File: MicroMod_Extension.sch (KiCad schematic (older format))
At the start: 79 parts, among them J1 2199230-4, J11 Screw_Terminal_01x04, J2 XKB_U262-16XN-4BVC11, J3 RSP-122811-01, J4 Screw_Terminal_01x04, J5 Conn_01x08, J6 Conn_01x08, J7 Conn_01x04, J8 Conn_01x04, J9 Conn_01x04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

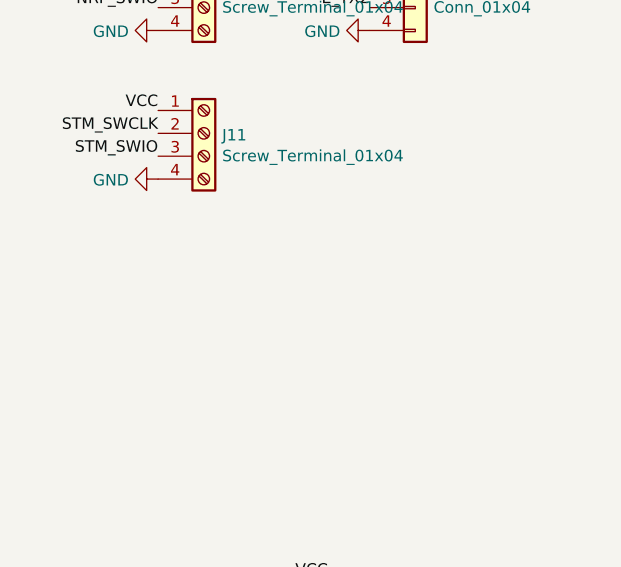
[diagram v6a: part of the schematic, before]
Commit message: add i2c connector
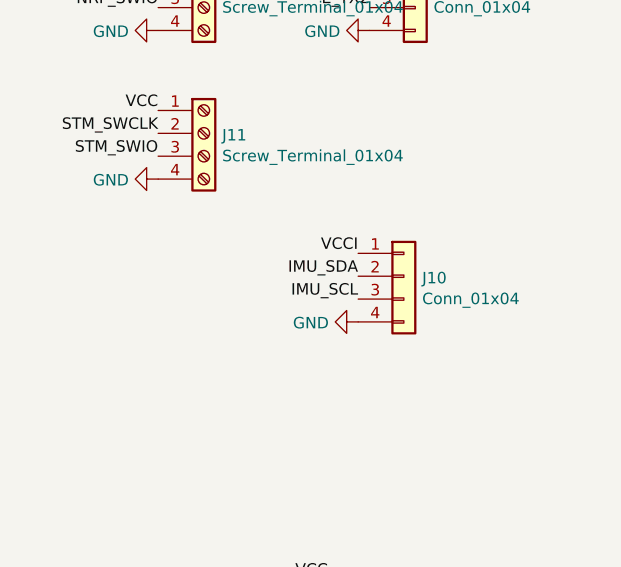
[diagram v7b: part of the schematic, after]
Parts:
- added J10: Conn_01x04, Connector_JST:JST_SUR_SM04B-SURS-TF_1x04-1MP_P0.80mm_Horizontal, symbol Connector_Generic:Conn_01x04
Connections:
- net GND: now also J10.4 (Pin_4)
- net IMU_SCL: now also J10.3 (Pin_3)
- net IMU_SDA: now also J10.2 (Pin_2)
- net VCCI: now also J10.1 (Pin_1)
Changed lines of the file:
@@
 NoConn ~ 12050 2825
 NoConn ~ 12050 1925
-NoConn ~ 5625 5975
-NoConn ~ 4425 5975
-NoConn ~ 4425 6675
-NoConn ~ 4425 6775
-Wire Wire Line
-	5625 6975 5725 6975
-Wire Wire Line
-	5725 6975 5725 7075
-Wire Wire Line
-	5625 7075 5725 7075
-Connection ~ 5725 7075
-Wire Wire Line
-	5725 7075 5725 7225
-$Comp
-L power:GND #PWR0131
-U 1 1 619EDD8D
-P 5725 7300
-F 0 "#PWR0131" H 5725 7050 50  0001 C CNN
-F 1 "GND" V 5730 7172 50  0000 R CNN
-F 2 "" H 5725 7300 50  0001 C CNN
-F 3 "" H 5725 7300 50  0001 C CNN
-	1    5725 7300
-	1    0    0    -1
-$EndComp
-Wire Wire Line
-	5625 5775 5675 5775
-Wire Wire Line
-	5675 5675 5625 5675
-Wire Wire Line
-	5675 5675 5850 5675
-Connection ~ 5675 5675
-$Comp
-L Device:C C1
-U 1 1 61A296B8
-P 5850 5825
-F 0 "C1" H 5875 5725 50  0000 L CNN
-F 1 "100n" H 5875 5650 50  0000 L CNN
-F 2 "Capacitor_SMD:C_0402_1005Metric" H 5888 5675 50  0001 C CNN
-F 3 "~" H 5850 5825 50  0001 C CNN
-	1    5850 5825
-	1    0    0    -1
-$EndComp
-Wire Wire Line
-	5725 6975 5725 6300
-Wire Wire Line
-	5725 6300 5850 6300
-Wire Wire Line
-	5850 6300 5850 5975
-Connection ~ 5725 6975
-Text Label 6225 5675 0    50   ~ 0
-VCCI
-Wire Wire Line
-	5675 5775 5675 5675
-Text Label 4425 6375 2    50   ~ 0
-SPI2_MOSI
-Text Label 4425 6275 2    50   ~ 0
-SPI2_SCK
-Connection ~ 5725 7225
-Wire Wire Line
-	5725 7225 5725 7300
-Text Label 5625 6775 0    50   ~ 0
-INT_GYR
-NoConn ~ 5625 6675
 Wire Wire Line
 	10550 9100 11425 9100
@@
 Text Label 12175 9100 0    50   ~ 0
 VCCI
-$Comp
-L MicroMod_Extension:BMP384 U8
-U 1 1 61BB569C
-P 6425 6350
-F 0 "U8" V 5975 5575 50  0000 C CNN
-F 1 "BMP384" V 5900 5475 50  0000 C CNN
-F 2 "MicroMod_Extension:PQFN45P200X200X100-10N" H 6275 6600 50  0001 C CNN
-F 3 "" H 6275 6600 50  0001 C CNN
-	1    6425 6350
-	0    -1   -1   0
-$EndComp
-Wire Wire Line
-	6475 6300 6475 5900
-Wire Wire Line
-	6475 5900 6775 5900
-Connection ~ 6475 5900
-$Comp
-L Device:C C23
-U 1 1 61BEE553
-P 6225 5825
-F 0 "C23" H 6125 5925 50  0000 L CNN
-F 1 "100n" H 6025 6000 50  0000 L CNN
-F 2 "Capacitor_SMD:C_0402_1005Metric" H 6263 5675 50  0001 C CNN
-F 3 "~" H 6225 5825 50  0001 C CNN
-	1    6225 5825
-	-1   0    0    1
-$EndComp
-Wire Wire Line
-	7075 5900 6925 5900
-Connection ~ 7075 5900
-NoConn ~ 7325 6250
-Text Label 6475 6500 2    50   ~ 0
-IMU_SCL
-Text Label 6925 6850 3    50   ~ 0
-IMU_SDA
-Wire Wire Line
-	7325 6500 7400 6500
-$Comp
-L power:GND #PWR0132
-U 1 1 61DA92BC
-P 7675 5900
-F 0 "#PWR0132" H 7675 5650 50  0001 C CNN
-F 1 "GND" V 7680 5772 50  0000 R CNN
-F 2 "" H 7675 5900 50  0001 C CNN
-F 3 "" H 7675 5900 50  0001 C CNN
-	1    7675 5900
-	0    -1   -1   0
-$EndComp
-Wire Wire Line
-	5850 5675 6225 5675
-Connection ~ 5850 5675
-Connection ~ 6475 5675
-Wire Wire Line
-	6475 5675 6475 5800
-Wire Wire Line
-	6475 5675 7400 5675
-Connection ~ 6225 5675
-Wire Wire Line
-	6225 5675 6475 5675
-Wire Wire Line
-	7075 5900 7675 5900
-Wire Wire Line
-	6225 5975 6225 6300
-Wire Wire Line
-	6225 6300 5850 6300
-Connection ~ 5850 6300
-Wire Wire Line
-	6775 6850 6775 7225
-$Comp
-L Device:C C24
-U 1 1 61EF129D
-P 6850 5800
-F 0 "C24" H 6750 5900 50  0000 L CNN
-F 1 "100n" H 6650 5975 50  0000 L CNN
-F 2 "Capacitor_SMD:C_0402_1005Metric" H 6888 5650 50  0001 C CNN
-F 3 "~" H 6850 5800 50  0001 C CNN
-	1    6850 5800
-	0    1    1    0
-$EndComp
-Wire Wire Line
-	6475 5800 6700 5800
-Connection ~ 6475 5800
-Wire Wire Line
-	6475 5800 6475 5900
-Wire Wire Line
-	7400 5675 7400 6500
-Wire Wire Line
-	7000 5800 7075 5800
-Wire Wire Line
-	7075 5800 7075 5900
-Wire Wire Line
-	6775 7225 5725 7225
-Wire Wire Line
-	7075 6850 7075 7025
-Wire Wire Line
-	7075 7025 7400 7025
-Wire Wire Line
-	7400 7025 7400 6500
-Connection ~ 7400 6500
 Connection ~ 2050 7200
 Connection ~ 2050 7000
@@
 	1    0    0    -1
 $EndComp
-Text Label 4425 6475 2    50   ~ 0
-SPI2_MISO
+Text Label 15225 2275 2    50   ~ 0
+C4
+NoConn ~ 15225 2375
+Text Label 4425 6075 2    50   ~ 0
+C13
 $Comp
 L MicroMod_Extension:BMI270 U7
@@
 	1    0    0    -1
 $EndComp
-Text Label 4425 6075 2    50   ~ 0
-C13
-Text Label 15225 2275 2    50   ~ 0
-C4
-NoConn ~ 15225 2375
+Text Label 4425 6475 2    50   ~ 0
+SPI2_MISO
+Connection ~ 7400 6500
+Wire Wire Line
+	7400 7025 7400 6500
+Wire Wire Line
+	7075 7025 7400 7025
+Wire Wire Line
+	7075 6850 7075 7025
+Wire Wire Line
+	6775 7225 5725 7225
+Wire Wire Line
+	7075 5800 7075 5900
+Wire Wire Line
+	7000 5800 7075 5800
+Wire Wire Line
+	7400 5675 7400 6500
+Wire Wire Line
+	6475 5800 6475 5900
+Connection ~ 6475 5800
+Wire Wire Line
+	6475 5800 6700 5800
+$Comp
+L Device:C C24
+U 1 1 61EF129D
+P 6850 5800
+F 0 "C24" H 6750 5900 50  0000 L CNN
+F 1 "100n" H 6650 5975 50  0000 L CNN
+F 2 "Capacitor_SMD:C_0402_1005Metric" H 6888 5650 50  0001 C CNN
+F 3 "~" H 6850 5800 50  0001 C CNN
+	1    6850 5800
+	0    1    1    0
+$EndComp
+Wire Wire Line
+	6775 6850 6775 7225
+Connection ~ 5850 6300
+Wire Wire Line
+	6225 6300 5850 6300
+Wire Wire Line
+	6225 5975 6225 6300
+Wire Wire Line
+	7075 5900 7675 5900
+Wire Wire Line
+	6225 5675 6475 5675
+Connection ~ 6225 5675
+Wire Wire Line
+	6475 5675 7400 5675
+Wire Wire Line
+	6475 5675 6475 5800
+Connection ~ 6475 5675
+Connection ~ 5850 5675
+Wire Wire Line
+	5850 5675 6225 5675
+$Comp
+L power:GND #PWR0132
+U 1 1 61DA92BC
+P 7675 5900
+F 0 "#PWR0132" H 7675 5650 50  0001 C CNN
+F 1 "GND" V 7680 5772 50  0000 R CNN
+F 2 "" H 7675 5900 50  0001 C CNN
+F 3 "" H 7675 5900 50  0001 C CNN
+	1    7675 5900
+	0    -1   -1   0
+$EndComp
+Wire Wire Line
+	7325 6500 7400 6500
+Text Label 6925 6850 3    50   ~ 0
+IMU_SDA
+Text Label 6475 6500 2    50   ~ 0
+IMU_SCL
+NoConn ~ 7325 6250
+Connection ~ 7075 5900
+Wire Wire Line
+	7075 5900 6925 5900
+$Comp
+L Device:C C23
+U 1 1 61BEE553
+P 6225 5825
+F 0 "C23" H 6125 5925 50  0000 L CNN
+F 1 "100n" H 6025 6000 50  0000 L CNN
+F 2 "Capacitor_SMD:C_0402_1005Metric" H 6263 5675 50  0001 C CNN
+F 3 "~" H 6225 5825 50  0001 C CNN
+	1    6225 5825
+	-1   0    0    1
+$EndComp
+Connection ~ 6475 5900
+Wire Wire Line
+	6475 5900 6775 5900
+Wire Wire Line
+	6475 6300 6475 5900
+$Comp
+L MicroMod_Extension:BMP384 U8
+U 1 1 61BB569C
+P 6425 6350
+F 0 "U8" V 5975 5575 50  0000 C CNN
+F 1 "BMP384" V 5900 5475 50  0000 C CNN
+F 2 "MicroMod_Extension:PQFN45P200X200X100-10N" H 6275 6600 50  0001 C CNN
+F 3 "" H 6275 6600 50  0001 C CNN
+	1    6425 6350
+	0    -1   -1   0
+$EndComp
+NoConn ~ 5625 6675
+Text Label 5625 6775 0    50   ~ 0
+INT_GYR
+Wire Wire Line
+	5725 7225 5725 7300
+Connection ~ 5725 7225
+Text Label 4425 6275 2    50   ~ 0
+SPI2_SCK
+Text Label 4425 6375 2    50   ~ 0
+SPI2_MOSI
+Wire Wire Line
+	5675 5775 5675 5675
+Text Label 6225 5675 0    50   ~ 0
+VCCI
+Connection ~ 5725 6975
+Wire Wire Line
+	5850 6300 5850 5975
+Wire Wire Line
+	5725 6300 5850 6300
+Wire Wire Line
+	5725 6975 5725 6300
+$Comp
+L Device:C C1
+U 1 1 61A296B8
+P 5850 5825
+F 0 "C1" H 5875 5725 50  0000 L CNN
+F 1 "100n" H 5875 5650 50  0000 L CNN
+F 2 "Capacitor_SMD:C_0402_1005Metric" H 5888 5675 50  0001 C CNN
+F 3 "~" H 5850 5825 50  0001 C CNN
+	1    5850 5825
+	1    0    0    -1
+$EndComp
+Connection ~ 5675 5675
+Wire Wire Line
+	5675 5675 5850 5675
+Wire Wire Line
+	5675 5675 5625 5675
+Wire Wire Line
+	5625 5775 5675 5775
+$Comp
+L power:GND #PWR0131
+U 1 1 619EDD8D
+P 5725 7300
+F 0 "#PWR0131" H 5725 7050 50  0001 C CNN
+F 1 "GND" V 5730 7172 50  0000 R CNN
+F 2 "" H 5725 7300 50  0001 C CNN
+F 3 "" H 5725 7300 50  0001 C CNN
+	1    5725 7300
+	1    0    0    -1
+$EndComp
+Wire Wire Line
+	5725 7075 5725 7225
+Connection ~ 5725 7075
+Wire Wire Line
+	5625 7075 5725 7075
+Wire Wire Line
+	5725 6975 5725 7075
+Wire Wire Line
+	5625 6975 5725 6975
+NoConn ~ 4425 6775
+NoConn ~ 4425 6675
+NoConn ~ 4425 5975
+NoConn ~ 5625 5975
+Text Label 15000 4700 2    50   ~ 0
+IMU_SDA
+Text Label 15000 4800 2    50   ~ 0
+IMU_SCL
+$Comp
+L power:GND #PWR01
+U 1 1 62E5D741
+P 15000 4900
+F 0 "#PWR01" H 15000 4650 50  0001 C CNN
+F 1 "GND" V 15005 4772 50  0000 R CNN
+F 2 "" H 15000 4900 50  0001 C CNN
+F 3 "" H 15000 4900 50  0001 C CNN
+	1    15000 4900
+	0    1    1    0
+$EndComp
+$Comp
+L Connector_Generic:Conn_01x04 J10
+U 1 1 62E5D747
+P 15200 4700
+F 0 "J10" H 15280 4692 50  0000 L CNN
+F 1 "Conn_01x04" H 15280 4601 50  0000 L CNN
+F 2 "Connector_JST:JST_SUR_SM04B-SURS-TF_1x04-1MP_P0.80mm_Horizontal" H 15200 4700 50  0001 C CNN
+F 3 "~" H 15200 4700 50  0001 C CNN
+	1    15200 4700
+	1    0    0    -1
+$EndComp
+Text Label 15000 4600 2    50   ~ 0
+VCCI
 $EndSCHEMATC
